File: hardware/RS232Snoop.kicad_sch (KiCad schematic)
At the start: 5 parts, among them J3 Conn_01x02, J4 Screw_Terminal_01x03, J5 Screw_Terminal_01x03

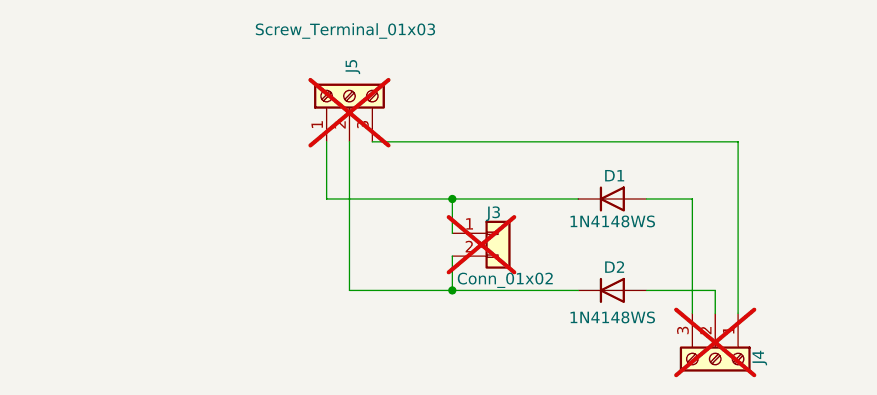
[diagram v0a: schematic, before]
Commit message: Added headers for straight or crossover
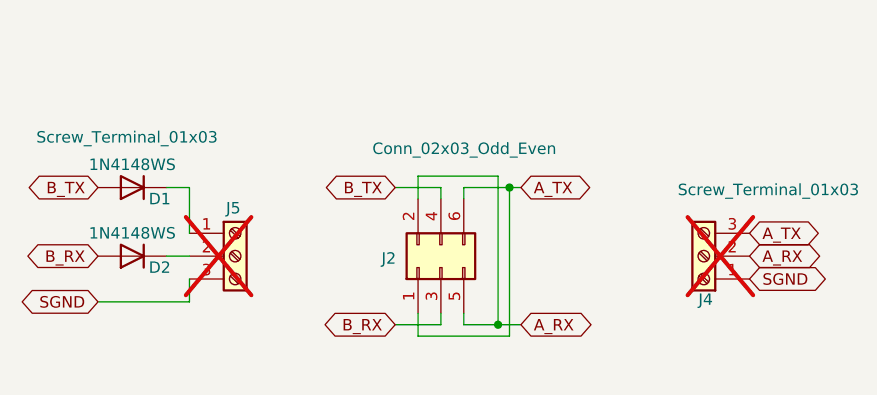
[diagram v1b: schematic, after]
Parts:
- removed J3: Conn_01x02, Connector_PinHeader_1.27mm:PinHeader_1x02_P1.27mm_Vertical, symbol Connector_Generic:Conn_01x02
- added J2: Conn_02x03_Odd_Even, Connector_PinHeader_2.54mm:PinHeader_2x03_P2.54mm_Vertical, symbol Connector_Generic:Conn_02x03_Odd_Even
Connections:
- net A_TX: now reaches J4.3 (Pin_3)
- net A_TX: now also J2.1 (Pin_1), J2.6 (Pin_6); no longer D1.2 (A)
- net SGND: now reaches J4.1 (Pin_1), J5.3 (Pin_3)
- net A_RX: now reaches J4.2 (Pin_2)
- net A_RX: now also J2.2 (Pin_2), J2.5 (Pin_5); no longer D2.2 (A)
- new net B_RX: D2.2 (A), J2.3 (Pin_3)
- new net B_TX: D1.2 (A), J2.4 (Pin_4)
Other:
- moved on the sheet: D1, D2, J4, J5
